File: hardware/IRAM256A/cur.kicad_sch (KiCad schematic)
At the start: 9 parts

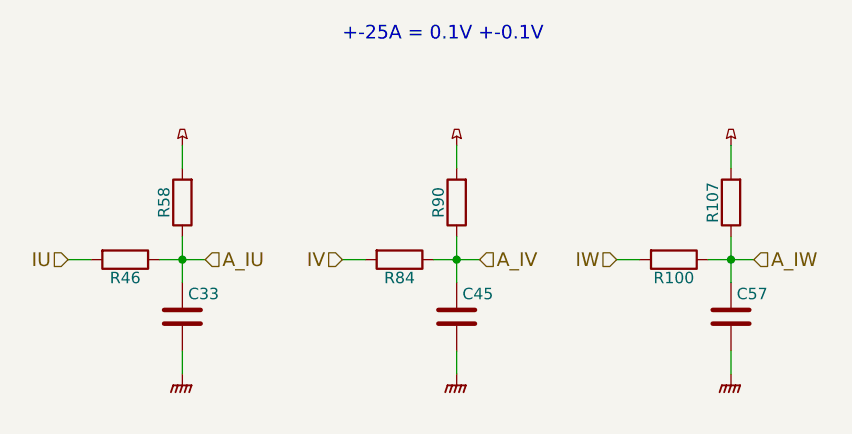
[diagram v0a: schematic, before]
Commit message: Structure change + kicad 3d models updated
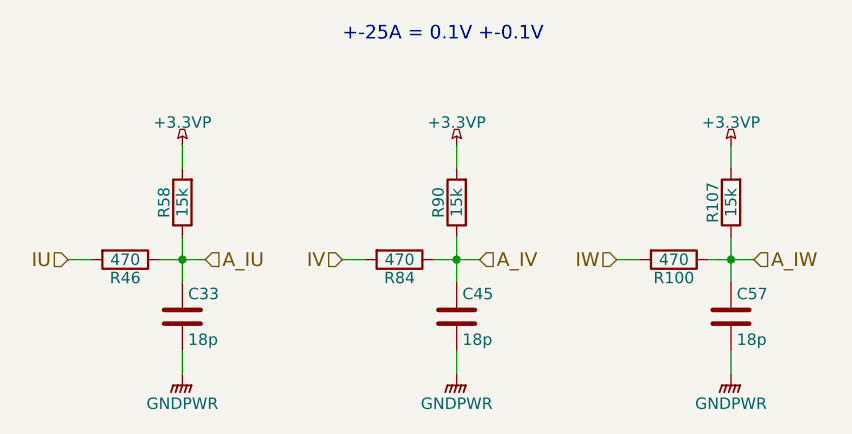
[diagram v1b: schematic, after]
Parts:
- C33, C45, C57: value (none) -> 18p; footprint (none) -> stmbl:C_0603
- R100, R46, R84: value (none) -> 470; footprint (none) -> stmbl:R_0603
- R107, R58, R90: value (none) -> 15k; footprint (none) -> stmbl:R_0603
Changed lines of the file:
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@@
       (effects (font (size 1.27 1.27)) hide)
     )
-    (property "Value" "" (id 1) (at 119.38 60.96 0))
+    (property "Value" "+3.3VP" (id 1) (at 119.38 60.96 0))
     (property "Footprint" "" (id 2) (at 119.38 63.5 0))
     (property "Datasheet" "" (id 3) (at 119.38 63.5 0))
@@
       (effects (font (size 1.27 1.27)) hide)
     )
-    (property "Value" "" (id 1) (at 119.38 92.202 0))
+    (property "Value" "GNDPWR" (id 1) (at 119.38 92.202 0))
     (property "Footprint" "" (id 2) (at 119.38 90.17 0))
     (property "Datasheet" "" (id 3) (at 119.38 90.17 0))
@@
     (in_bom yes) (on_board yes)
     (property "Reference" "R46" (id 0) (at 113.03 78.232 90))
-    (property "Value" "" (id 1) (at 113.03 76.2 90))
-    (property "Footprint" "" (id 2) (at 113.03 74.422 90)
+    (property "Value" "470" (id 1) (at 113.03 76.2 90))
+    (property "Footprint" "stmbl:R_0603" (id 2) (at 113.03 74.422 90)
       (effects (font (size 1.27 1.27)) hide)
     )
@@
       (effects (font (size 1.27 1.27)) (justify left))
     )
-    (property "Value" "" (id 1) (at 120.015 85.09 0)
-      (effects (font (size 1.27 1.27)) (justify left))
-    )
-    (property "Footprint" "" (id 2) (at 120.3452 86.36 0)
+    (property "Value" "18p" (id 1) (at 120.015 85.09 0)
+      (effects (font (size 1.27 1.27)) (justify left))
+    )
+    (property "Footprint" "stmbl:C_0603" (id 2) (at 120.3452 86.36 0)
       (effects (font (size 1.27 1.27)) hide)
     )
@@
     (in_bom yes) (on_board yes)
     (property "Reference" "R58" (id 0) (at 117.348 69.85 90))
-    (property "Value" "" (id 1) (at 119.38 69.85 90))
-    (property "Footprint" "" (id 2) (at 121.158 69.85 90)
+    (property "Value" "15k" (id 1) (at 119.38 69.85 90))
+    (property "Footprint" "stmbl:R_0603" (id 2) (at 121.158 69.85 90)
       (effects (font (size 1.27 1.27)) hide)
     )
@@
       (effects (font (size 1.27 1.27)) hide)
     )
-    (property "Value" "" (id 1) (at 149.86 60.96 0))
+    (property "Value" "+3.3VP" (id 1) (at 149.86 60.96 0))
     (property "Footprint" "" (id 2) (at 149.86 63.5 0))
     (property "Datasheet" "" (id 3) (at 149.86 63.5 0))
@@
       (effects (font (size 1.27 1.27)) hide)
     )
-    (property "Value" "" (id 1) (at 149.86 92.202 0))
+    (property "Value" "GNDPWR" (id 1) (at 149.86 92.202 0))
     (property "Footprint" "" (id 2) (at 149.86 90.17 0))
     (property "Datasheet" "" (id 3) (at 149.86 90.17 0))
@@
     (in_bom yes) (on_board yes)
     (property "Reference" "R84" (id 0) (at 143.51 78.232 90))
-    (property "Value" "" (id 1) (at 143.51 76.2 90))
-    (property "Footprint" "" (id 2) (at 143.51 74.422 90)
+    (property "Value" "470" (id 1) (at 143.51 76.2 90))
+    (property "Footprint" "stmbl:R_0603" (id 2) (at 143.51 74.422 90)
       (effects (font (size 1.27 1.27)) hide)
     )
@@
       (effects (font (size 1.27 1.27)) (justify left))
     )
-    (property "Value" "" (id 1) (at 150.495 85.09 0)
-      (effects (font (size 1.27 1.27)) (justify left))
-    )
-    (property "Footprint" "" (id 2) (at 150.8252 86.36 0)
+    (property "Value" "18p" (id 1) (at 150.495 85.09 0)
+      (effects (font (size 1.27 1.27)) (justify left))
+    )
+    (property "Footprint" "stmbl:C_0603" (id 2) (at 150.8252 86.36 0)
       (effects (font (size 1.27 1.27)) hide)
     )
@@
     (in_bom yes) (on_board yes)
     (property "Reference" "R90" (id 0) (at 147.828 69.85 90))
-    (property "Value" "" (id 1) (at 149.86 69.85 90))
-    (property "Footprint" "" (id 2) (at 151.638 69.85 90)
+    (property "Value" "15k" (id 1) (at 149.86 69.85 90))
+    (property "Footprint" "stmbl:R_0603" (id 2) (at 151.638 69.85 90)
       (effects (font (size 1.27 1.27)) hide)
     )
@@
       (effects (font (size 1.27 1.27)) hide)
     )
-    (property "Value" "" (id 1) (at 180.34 60.96 0))
+    (property "Value" "+3.3VP" (id 1) (at 180.34 60.96 0))
     (property "Footprint" "" (id 2) (at 180.34 63.5 0))
     (property "Datasheet" "" (id 3) (at 180.34 63.5 0))
@@
       (effects (font (size 1.27 1.27)) hide)
     )
-    (property "Value" "" (id 1) (at 180.34 92.202 0))
+    (property "Value" "GNDPWR" (id 1) (at 180.34 92.202 0))
     (property "Footprint" "" (id 2) (at 180.34 90.17 0))
     (property "Datasheet" "" (id 3) (at 180.34 90.17 0))
@@
     (in_bom yes) (on_board yes)
     (property "Reference" "R100" (id 0) (at 173.99 78.232 90))
-    (property "Value" "" (id 1) (at 173.99 76.2 90))
-    (property "Footprint" "" (id 2) (at 173.99 74.422 90)
+    (property "Value" "470" (id 1) (at 173.99 76.2 90))
+    (property "Footprint" "stmbl:R_0603" (id 2) (at 173.99 74.422 90)
       (effects (font (size 1.27 1.27)) hide)
     )
@@
       (effects (font (size 1.27 1.27)) (justify left))
     )
-    (property "Value" "" (id 1) (at 180.975 85.09 0)
-      (effects (font (size 1.27 1.27)) (justify left))
-    )
-    (property "Footprint" "" (id 2) (at 181.3052 86.36 0)
+    (property "Value" "18p" (id 1) (at 180.975 85.09 0)
+      (effects (font (size 1.27 1.27)) (justify left))
+    )
+    (property "Footprint" "stmbl:C_0603" (id 2) (at 181.3052 86.36 0)
       (effects (font (size 1.27 1.27)) hide)
     )
@@
     (in_bom yes) (on_board yes)
     (property "Reference" "R107" (id 0) (at 178.308 69.85 90))
-    (property "Value" "" (id 1) (at 180.34 69.85 90))
-    (property "Footprint" "" (id 2) (at 182.118 69.85 90)
-      (effects (font (size 1.27 1.27)) hide)
-    )
+    (property "Value" "15k" (id 1) (at 180.34 69.85 90))
+    (property "Footprint" "stmbl:R_0603" (id 2) (at 182.118 69.85 90)
+      (effects (font (size 1.27 1.27)) hide)
+    )
